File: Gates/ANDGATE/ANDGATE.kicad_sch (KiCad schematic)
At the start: 10 parts, among them U1 74AUP1G08

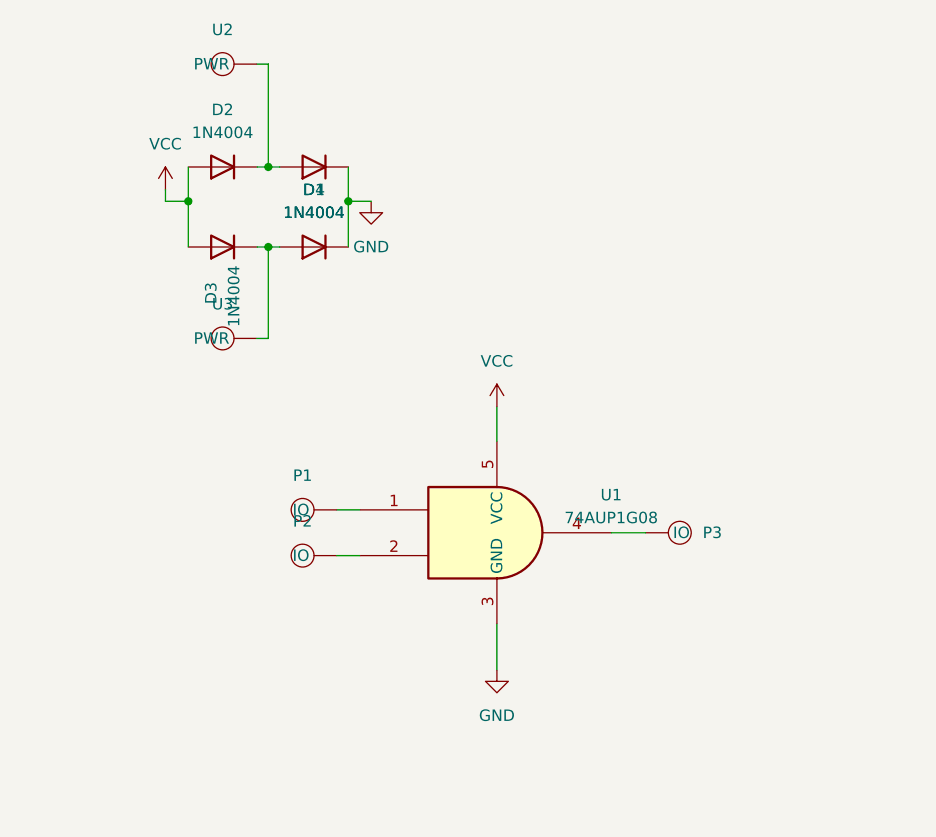
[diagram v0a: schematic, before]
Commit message: header pins and pcb start
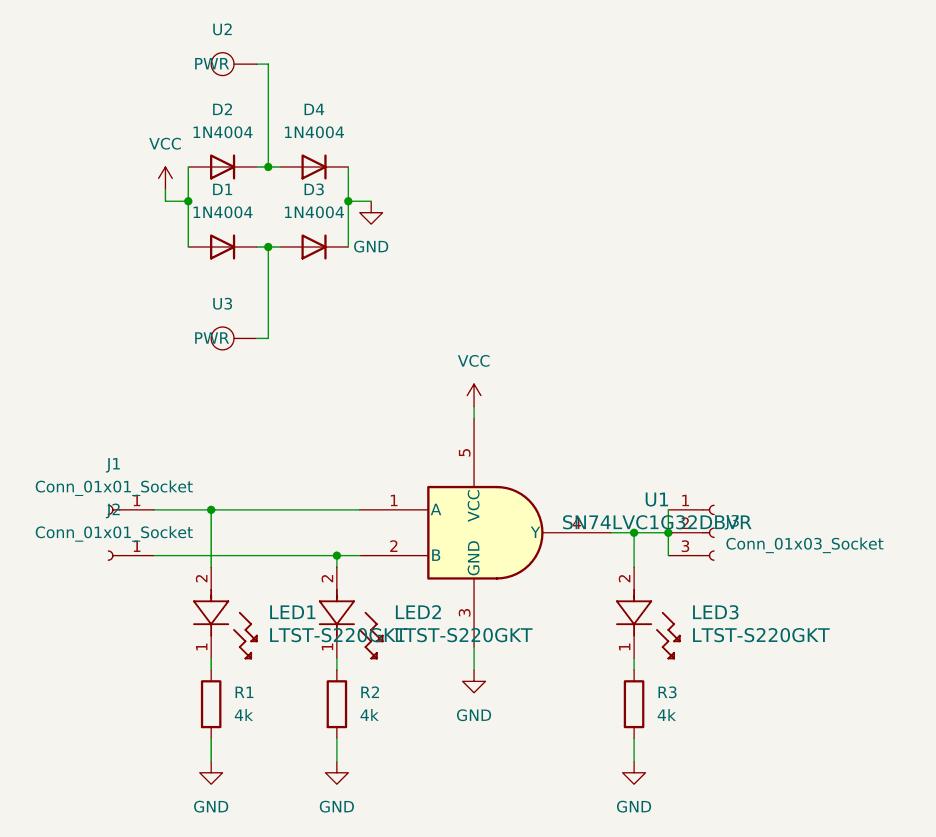
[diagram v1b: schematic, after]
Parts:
- removed P1, P2, P3: ~, symbol DigitalLogicLibrary:5mm_snap
- removed U1: 74AUP1G08, symbol DigitalLogicLibrary:74AUP1G08
- added J1, J2: Conn_01x01_Socket, Connector_PinHeader_1.00mm:PinHeader_1x01_P1.00mm_Vertical, symbol DigitalLogicLibrary:Conn_01x01_Socket
- added J3: Conn_01x03_Socket, Connector_PinHeader_1.00mm:PinHeader_1x03_P1.00mm_Vertical, symbol DigitalLogicLibrary:Conn_01x03_Socket
- added LED1, LED2, LED3: LTST-S220GKT, LED_SMD:LED_0603_1608Metric, symbol DigitalLogicLibrary:LTST-S220GKT
- added R1, R2, R3: 4k, Resistor_SMD:R_0201_0603Metric, symbol Device:R
- added U1: SN74LVC1G32DBVR, DBV5, symbol DigitalLogicLibrary:SN74LVC1G32DBVR
- D1, D2, D3, D4: footprint Diode_THT:D_DO-41_SOD81_P10.16mm_Horizontal -> Diode_SMD:D_SMA
- U2, U3: footprint (none) -> DigitalLogicFootprints:8mm snap
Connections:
- net GND: now also D3.1 (K), R1.2, R2.2, R3.2, U1.3 (GND); no longer D1.1 (K)
- net VCC: now also D1.2 (A), U1.5 (VCC); no longer D3.2 (A)
- net at D2.1 (K), U2. (PWR): now also D4.2 (A); no longer D1.2 (A)
- new net: D1.1 (K), D3.2 (A), U3. (PWR)
- new net: LED3.1, R3.1
- new net: J3.1 (Pin_1), J3.2 (Pin_2), J3.3 (Pin_3), LED3.2, U1.4 (Y)
- new net: J1.1 (Pin_1), LED1.2, U1.1 (A)
- new net: J2.1 (Pin_1), LED2.2, U1.2 (B)
- new net: LED2.1, R2.1
- new net: LED1.1, R1.1

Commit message: AND GATE passes DRC but with silk screen warnings
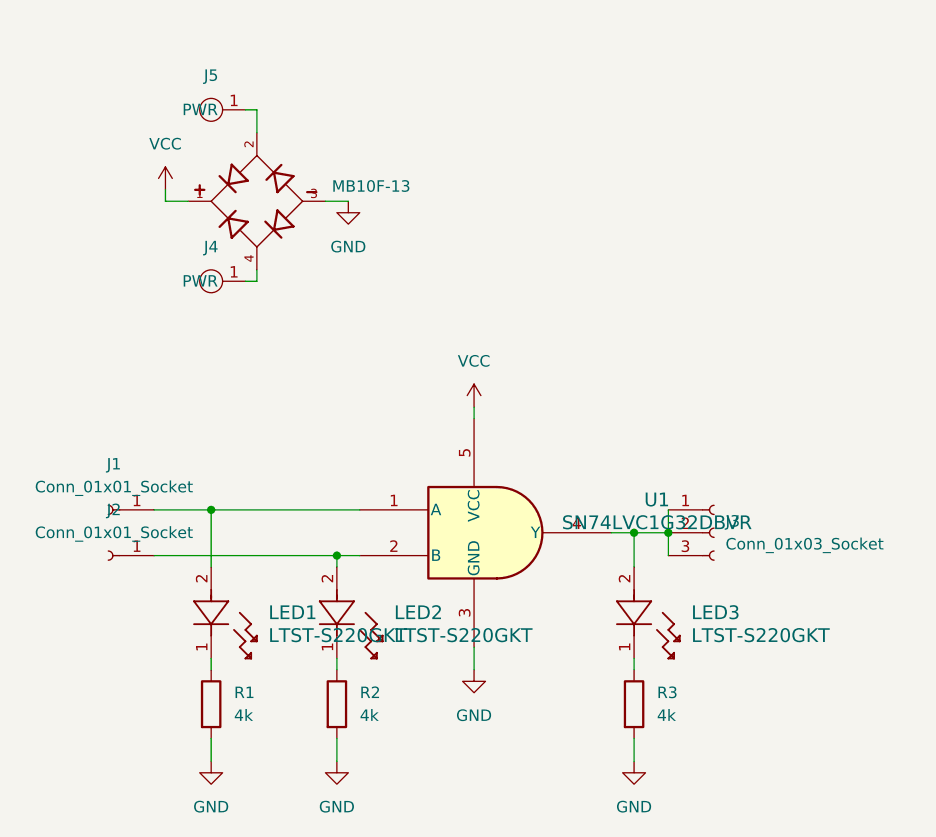
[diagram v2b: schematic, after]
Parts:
- removed D1, D2, D3, D4: 1N4004, Diode_SMD:D_SMA, symbol DigitalLogicLibrary:1N4004
- removed U2, U3: ~, DigitalLogicFootprints:8mm snap, symbol DigitalLogicLibrary:8mm_snap
- added D1: MB10F-13, DigitalLogicFootprints:DIOB_MB10F-13, symbol DigitalLogicLibrary:MB10F-13
- added J4, J5: ~, DigitalLogicFootprints:8mm-snap, symbol DigitalLogicLibrary:8mm_snap
- LED1, LED2, LED3: footprint LED_SMD:LED_0603_1608Metric -> LED_LTST-S220GKT_LTO
- R1, R2, R3: footprint Resistor_SMD:R_0201_0603Metric -> Resistor_SMD:R_0805_2012Metric_Pad1.20x1.40mm_HandSolder
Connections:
- net GND: now also D1.3
- net VCC: now also D1.1
- new net: D1.2, J5.1 (PWR)
- new net: D1.4, J4.1 (PWR)

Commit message: Changed pins to 2.54mm from 1mm
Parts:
- J1, J2: footprint Connector_PinHeader_1.00mm:PinHeader_1x01_P1.00mm_Vertical -> Connector_PinSocket_2.54mm:PinSocket_1x01_P2.54mm_Vertical
- J3: footprint Connector_PinHeader_1.00mm:PinHeader_1x03_P1.00mm_Vertical -> Connector_PinSocket_2.54mm:PinSocket_1x03_P2.54mm_Vertical
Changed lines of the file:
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@@
       (effects (font (size 1.27 1.27)) (justify left))
     )
-    (property "Footprint" "Connector_PinHeader_1.00mm:PinHeader_1x03_P1.00mm_Vertical" (at 157.48 101.6 0)
+    (property "Footprint" "Connector_PinSocket_2.54mm:PinSocket_1x03_P2.54mm_Vertical" (at 157.48 101.6 0)
       (effects (font (size 1.27 1.27)) hide)
     )
@@
       (effects (font (size 1.27 1.27)))
     )
-    (property "Footprint" "Connector_PinHeader_1.00mm:PinHeader_1x01_P1.00mm_Vertical" (at 90.17 104.14 0)
+    (property "Footprint" "Connector_PinSocket_2.54mm:PinSocket_1x01_P2.54mm_Vertical" (at 90.17 104.14 0)
       (effects (font (size 1.27 1.27)) hide)
     )
@@
       (effects (font (size 1.27 1.27)))
     )
-    (property "Footprint" "Connector_PinHeader_1.00mm:PinHeader_1x01_P1.00mm_Vertical" (at 90.17 99.06 0)
-      (effects (font (size 1.27 1.27)) hide)
-    )
+    (property "Footprint" "Connector_PinSocket_2.54mm:PinSocket_1x01_P2.54mm_Vertical" (at 90.17 99.06 0)
+      (effects (font (size 1.27 1.27)) hide)
+    )
